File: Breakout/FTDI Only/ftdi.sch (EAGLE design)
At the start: 28 parts, among them Q1 16Mhz, U5 93LC46BT-I/OT

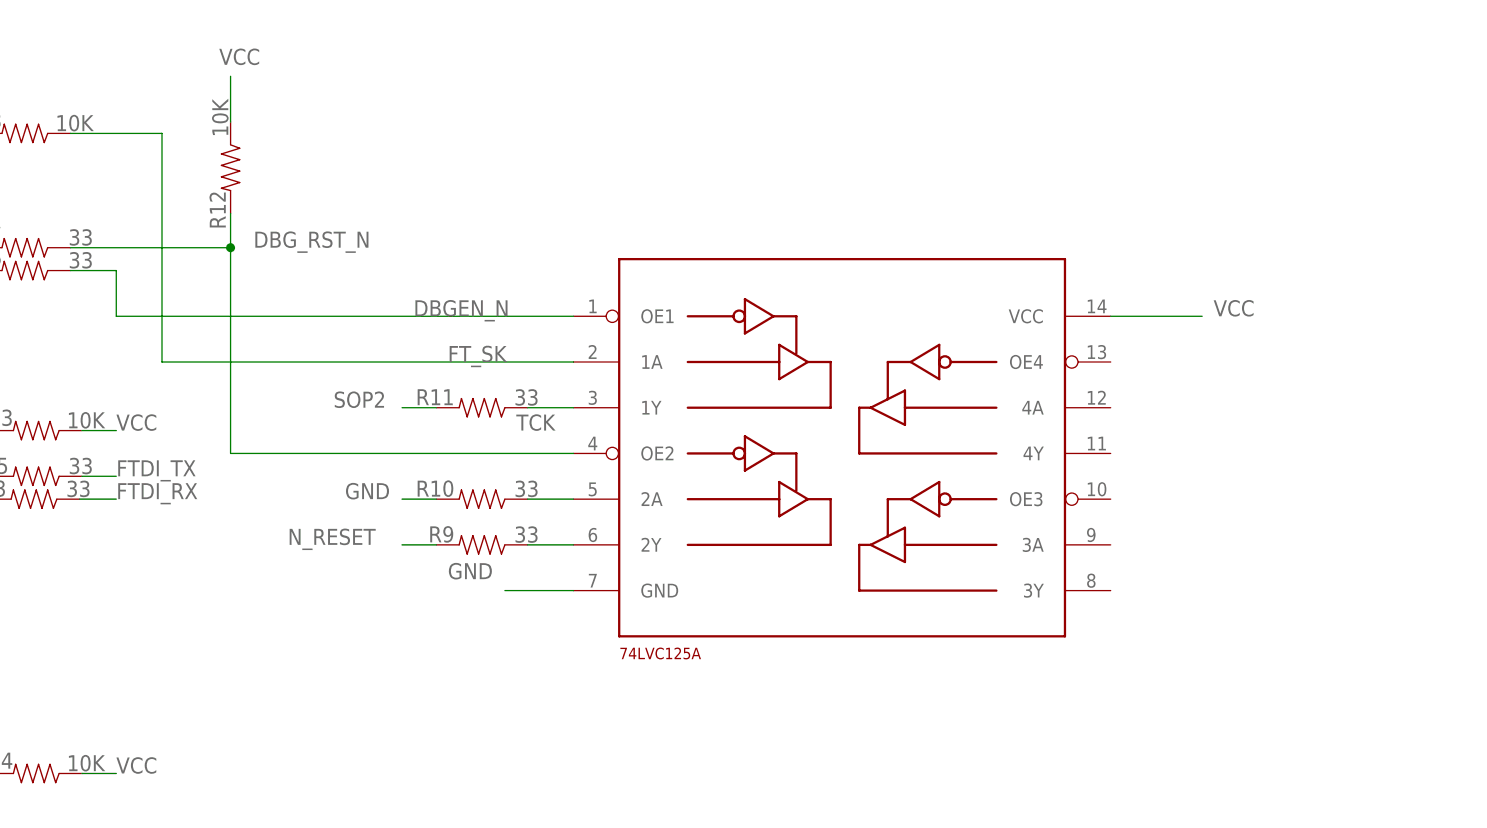
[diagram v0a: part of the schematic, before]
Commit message: replace chip
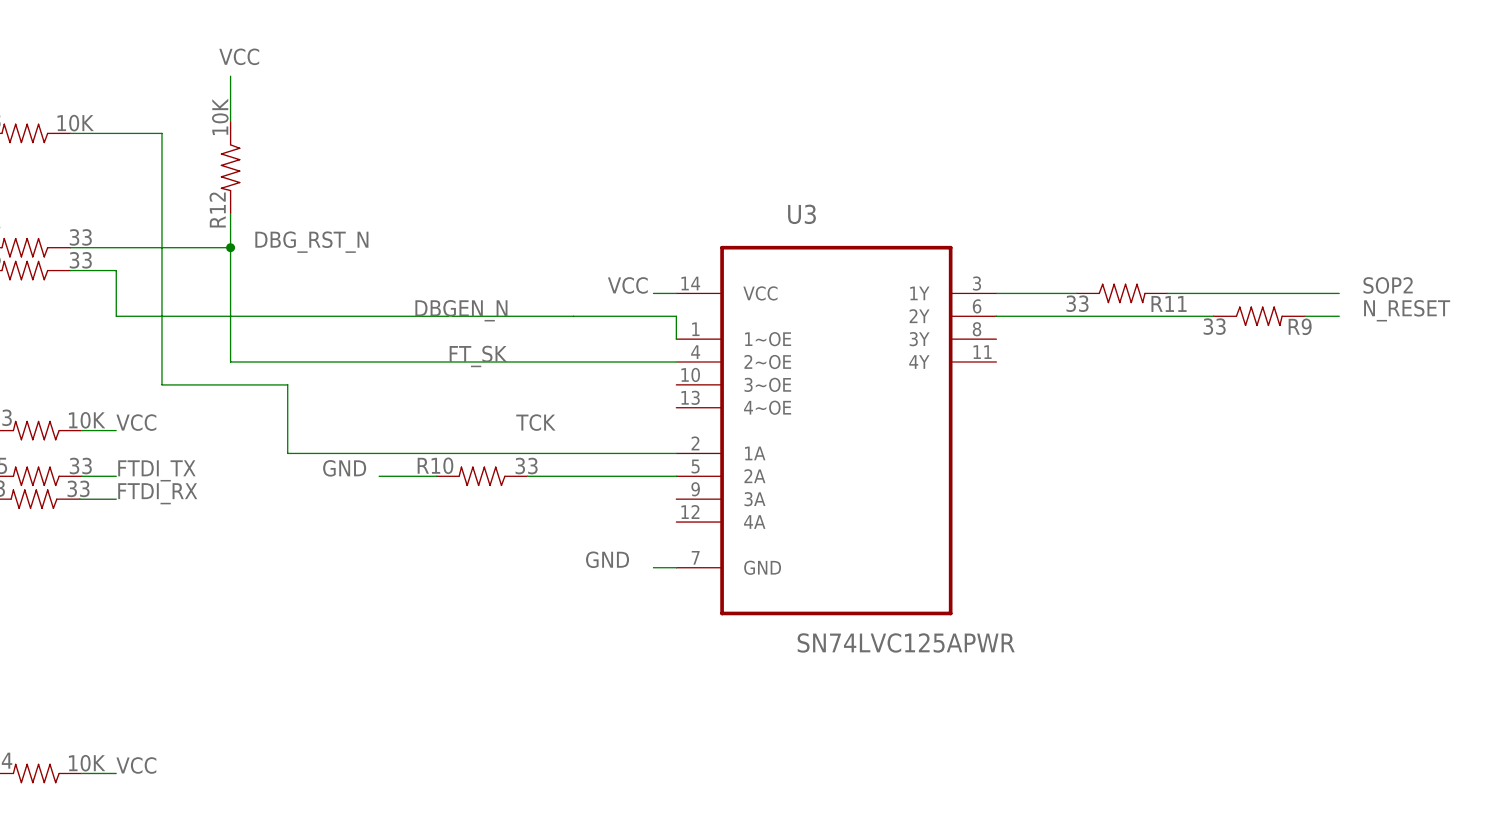
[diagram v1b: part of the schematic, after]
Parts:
- removed U$3: DECADE-74LVC125A, DECADE-libraries:DECADE-74LVC125A
- added U3: SN74LVC125APWR, Texas Instruments_By_element14_Batch_1:SN74LVC125APWR
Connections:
- net DBGEN_N: now also U3.1~OE; no longer U$3.OE1
- net DBG_RST_N: now also U3.2~OE; no longer U$3.OE2
- net FT_SK: now also U3.1A; no longer U$3.1A
- net GND: now also U3.GND; no longer U$3.GND
- net N$49: now also U3.2A; no longer U$3.2A
- net N$50: now also U3.2Y; no longer U$3.2Y
- net TCK: now also U3.1Y; no longer U$3.1Y
- net VCC: now also U3.VCC; no longer U$3.VCC
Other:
- moved on the sheet: R10, R11, R9
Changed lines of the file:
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@@
 <setting verticaltext="up"/>
 </settings>
-<grid distance="0.01" unitdist="inch" unit="inch" style="lines" multiple="1" display="no" altdistance="0.01" altunitdist="inch" altunit="inch"/>
+<grid distance="0.1" unitdist="inch" unit="inch" style="lines" multiple="1" display="no" altdistance="0.01" altunitdist="inch" altunit="inch"/>
 <layers>
 <layer number="1" name="Top" color="4" fill="1" visible="no" active="no"/>
@@
 <part name="C3" library="SparkFun-Passives" deviceset="CAP" device="0402-CAP" value="27pF"/>
 <part name="C4" library="SparkFun-Passives" deviceset="CAP" device="0402-CAP" value="33nF"/>
-<part name="U$3" library="DECADE-libraries" deviceset="DECADE-74LVC125A" device=""/>
 <part name="C5" library="SparkFun-Passives" deviceset="CAP" device="0402-CAP" value="0.1uF"/>
 <part name="L3" library="Spark" deviceset="INDUCTOR-SPARKFUN" device="0603"/>
@@
 <part name="R1" library="SparkFun-Passives" deviceset="RESISTOR" device="0402-RES" value="28"/>
 <part name="R15" library="SparkFun-Passives" deviceset="RESISTOR" device="0402-RES" value="28"/>
+<part name="U3" library="Texas Instruments_By_element14_Batch_1" deviceset="SN74LVC125APWR" device=""/>
 </parts>
 <sheets>
@@
 <instance part="C3" gate="G$1" x="55.88" y="309.88" rot="R90"/>
 <instance part="C4" gate="G$1" x="88.9" y="342.9" rot="R90"/>
-<instance part="U$3" gate="G$1" x="234.95" y="317.5"/>
 <instance part="C5" gate="G$1" x="68.58" y="355.6" rot="R90"/>
 <instance part="L3" gate="G$1" x="48.26" y="340.36" rot="R90"/>
@@
 <attribute name="VALUE" x="163.83" y="357.632" size="1.778" layer="96" rot="R180"/>
 </instance>
-<instance part="R9" gate="G$1" x="207.01" y="309.88" smashed="yes" rot="R180">
-<attribute name="NAME" x="203.962" y="311.9374" size="1.778" layer="95" rot="R180"/>
-<attribute name="VALUE" x="213.36" y="311.912" size="1.778" layer="96" rot="R180"/>
-</instance>
-<instance part="R10" gate="G$1" x="207.01" y="314.96" smashed="yes" rot="R180">
-<attribute name="NAME" x="203.962" y="317.0174" size="1.778" layer="95" rot="R180"/>
-<attribute name="VALUE" x="213.36" y="316.992" size="1.778" layer="96" rot="R180"/>
-</instance>
-<instance part="R11" gate="G$1" x="207.01" y="325.12" smashed="yes" rot="R180">
-<attribute name="NAME" x="203.962" y="327.1774" size="1.778" layer="95" rot="R180"/>
-<attribute name="VALUE" x="213.36" y="327.152" size="1.778" layer="96" rot="R180"/>
+<instance part="R9" gate="G$1" x="293.37" y="335.28" smashed="yes">
+<attribute name="NAME" x="296.418" y="333.2226" size="1.778" layer="95"/>
+<attribute name="VALUE" x="287.02" y="333.248" size="1.778" layer="96"/>
+</instance>
+<instance part="R10" gate="G$1" x="207.01" y="317.5" smashed="yes" rot="R180">
+<attribute name="NAME" x="203.962" y="319.5574" size="1.778" layer="95" rot="R180"/>
+<attribute name="VALUE" x="213.36" y="319.532" size="1.778" layer="96" rot="R180"/>
+</instance>
+<instance part="R11" gate="G$1" x="278.13" y="337.82" smashed="yes">
+<attribute name="NAME" x="281.178" y="335.7626" size="1.778" layer="95"/>
+<attribute name="VALUE" x="271.78" y="335.788" size="1.778" layer="96"/>
 </instance>
 <instance part="R12" gate="G$1" x="179.07" y="351.79" smashed="yes" rot="R270">
@@
 <attribute name="VALUE" x="55.88" y="350.012" size="1.778" layer="96" rot="R180"/>
 </instance>
+<instance part="U3" gate="A" x="246.38" y="325.12"/>
 </instances>
 <busses>
@@
 </segment>
 <segment>
-<pinref part="U$3" gate="G$1" pin="GND"/>
-<wire x1="217.17" y1="304.8" x2="209.55" y2="304.8" width="0.1524" layer="91"/>
-<label x="203.2" y="306.07" size="1.778" layer="95"/>
-</segment>
-<segment>
-<wire x1="201.93" y1="314.96" x2="198.12" y2="314.96" width="0.1524" layer="91"/>
-<label x="191.77" y="314.96" size="1.778" layer="95"/>
+<wire x1="201.93" y1="317.5" x2="195.58" y2="317.5" width="0.1524" layer="91"/>
+<label x="189.23" y="317.5" size="1.778" layer="95"/>
 <pinref part="R10" gate="G$1" pin="2"/>
 </segment>
@@
 <label x="63.5" y="280.67" size="1.778" layer="95"/>
 </segment>
+<segment>
+<pinref part="U3" gate="A" pin="GND"/>
+<wire x1="228.6" y1="307.34" x2="226.06" y2="307.34" width="0.1524" layer="91"/>
+<label x="218.44" y="307.34" size="1.778" layer="95"/>
+</segment>
 </net>
 <net name="VCC" class="0">
-<segment>
-<pinref part="U$3" gate="G$1" pin="VCC"/>
-<wire x1="276.86" y1="335.28" x2="287.02" y2="335.28" width="0.1524" layer="91"/>
-<label x="288.29" y="335.28" size="1.778" layer="95"/>
-</segment>
 <segment>
 <label x="177.8" y="363.22" size="1.778" layer="95"/>
@@
 <label x="166.37" y="284.48" size="1.778" layer="95"/>
 </segment>
+<segment>
+<pinref part="U3" gate="A" pin="VCC"/>
+<wire x1="228.6" y1="337.82" x2="226.06" y2="337.82" width="0.1524" layer="91"/>
+<label x="220.98" y="337.82" size="1.778" layer="95"/>
+</segment>
 </net>
 <net name="+5V_USB" class="0">
@@
 <net name="TCK" class="0">
 <segment>
-<pinref part="U$3" gate="G$1" pin="1Y"/>
-<wire x1="217.17" y1="325.12" x2="212.09" y2="325.12" width="0.1524" layer="91"/>
 <label x="210.82" y="322.58" size="1.778" layer="95"/>
 <pinref part="R11" gate="G$1" pin="1"/>
+<pinref part="U3" gate="A" pin="1Y"/>
+<wire x1="273.05" y1="337.82" x2="264.16" y2="337.82" width="0.1524" layer="91"/>
 </segment>
 </net>
 <net name="DBGEN_N" class="0">
 <segment>
-<pinref part="U$3" gate="G$1" pin="OE1"/>
 <label x="199.39" y="335.28" size="1.778" layer="95"/>
 <wire x1="161.29" y1="340.36" x2="166.37" y2="340.36" width="0.1524" layer="91"/>
 <wire x1="166.37" y1="340.36" x2="166.37" y2="335.28" width="0.1524" layer="91"/>
+<pinref part="R6" gate="G$1" pin="1"/>
 <wire x1="166.37" y1="335.28" x2="217.17" y2="335.28" width="0.1524" layer="91"/>
-<pinref part="R6" gate="G$1" pin="1"/>
+<wire x1="217.17" y1="335.28" x2="228.6" y2="335.28" width="0.1524" layer="91"/>
+<pinref part="U3" gate="A" pin="1~OE"/>
+<wire x1="228.6" y1="335.28" x2="228.6" y2="332.74" width="0.1524" layer="91"/>
 </segment>
 </net>
 <net name="FT_SK" class="0">
 <segment>
-<pinref part="U$3" gate="G$1" pin="1A"/>
 <label x="203.2" y="330.2" size="1.778" layer="95"/>
 <wire x1="161.29" y1="355.6" x2="171.45" y2="355.6" width="0.1524" layer="91"/>
-<wire x1="171.45" y1="355.6" x2="171.45" y2="330.2" width="0.1524" layer="91"/>
-<wire x1="171.45" y1="330.2" x2="217.17" y2="330.2" width="0.1524" layer="91"/>
+<wire x1="171.45" y1="355.6" x2="171.45" y2="327.66" width="0.1524" layer="91"/>
+<wire x1="171.45" y1="327.66" x2="185.42" y2="327.66" width="0.1524" layer="91"/>
 <pinref part="R8" gate="G$1" pin="1"/>
+<wire x1="185.42" y1="327.66" x2="185.42" y2="320.04" width="0.1524" layer="91"/>
+<pinref part="U3" gate="A" pin="1A"/>
+<wire x1="185.42" y1="320.04" x2="228.6" y2="320.04" width="0.1524" layer="91"/>
 </segment>
 </net>
@@
 <net name="SOP2" class="0">
 <segment>
-<wire x1="201.93" y1="325.12" x2="198.12" y2="325.12" width="0.1524" layer="91"/>
-<label x="190.5" y="325.12" size="1.778" layer="95"/>
+<wire x1="283.21" y1="337.82" x2="302.26" y2="337.82" width="0.1524" layer="91"/>
+<label x="304.8" y="337.82" size="1.778" layer="95"/>
 <pinref part="R11" gate="G$1" pin="2"/>
 </segment>
@@
 <wire x1="161.29" y1="342.9" x2="179.07" y2="342.9" width="0.1524" layer="91"/>
 <wire x1="179.07" y1="342.9" x2="179.07" y2="346.71" width="0.1524" layer="91"/>
-<wire x1="179.07" y1="342.9" x2="179.07" y2="320.04" width="0.1524" layer="91"/>
-<pinref part="U$3" gate="G$1" pin="OE2"/>
-<wire x1="179.07" y1="320.04" x2="217.17" y2="320.04" width="0.1524" layer="91"/>
+<wire x1="179.07" y1="342.9" x2="179.07" y2="330.2" width="0.1524" layer="91"/>
 <label x="181.61" y="342.9" size="1.778" layer="95"/>
 <junction x="179.07" y="342.9"/>
 <pinref part="R7" gate="G$1" pin="1"/>
 <pinref part="R12" gate="G$1" pin="2"/>
+<pinref part="U3" gate="A" pin="2~OE"/>
+<wire x1="179.07" y1="330.2" x2="228.6" y2="330.2" width="0.1524" layer="91"/>
 </segment>
 </net>
 <net name="N$49" class="0">
 <segment>
-<pinref part="U$3" gate="G$1" pin="2A"/>
-<wire x1="212.09" y1="314.96" x2="217.17" y2="314.96" width="0.1524" layer="91"/>
 <pinref part="R10" gate="G$1" pin="1"/>
+<wire x1="212.09" y1="317.5" x2="228.6" y2="317.5" width="0.1524" layer="91"/>
+<pinref part="U3" gate="A" pin="2A"/>
 </segment>
 </net>
 <net name="N$50" class="0">
 <segment>
-<pinref part="U$3" gate="G$1" pin="2Y"/>
-<wire x1="212.09" y1="309.88" x2="217.17" y2="309.88" width="0.1524" layer="91"/>
 <pinref part="R9" gate="G$1" pin="1"/>
+<pinref part="U3" gate="A" pin="2Y"/>
+<wire x1="288.29" y1="335.28" x2="264.16" y2="335.28" width="0.1524" layer="91"/>
 </segment>
 </net>
 <net name="N_RESET" class="0">
 <segment>
-<wire x1="201.93" y1="309.88" x2="198.12" y2="309.88" width="0.1524" layer="91"/>
-<label x="185.42" y="309.88" size="1.778" layer="95"/>
+<wire x1="298.45" y1="335.28" x2="302.26" y2="335.28" width="0.1524" layer="91"/>
+<label x="304.8" y="335.28" size="1.778" layer="95"/>
 <pinref part="R9" gate="G$1" pin="2"/>
 </segment>
